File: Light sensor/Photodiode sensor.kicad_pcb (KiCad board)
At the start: 2 copper layers, 29.2 x 22.6 mm, 23 parts, among them IC1 MCP6002-E_MS, IC2 MCP6002-E_MS, J1 Conn_01x02, J2 Conn_01x05, J3 Conn_01x04

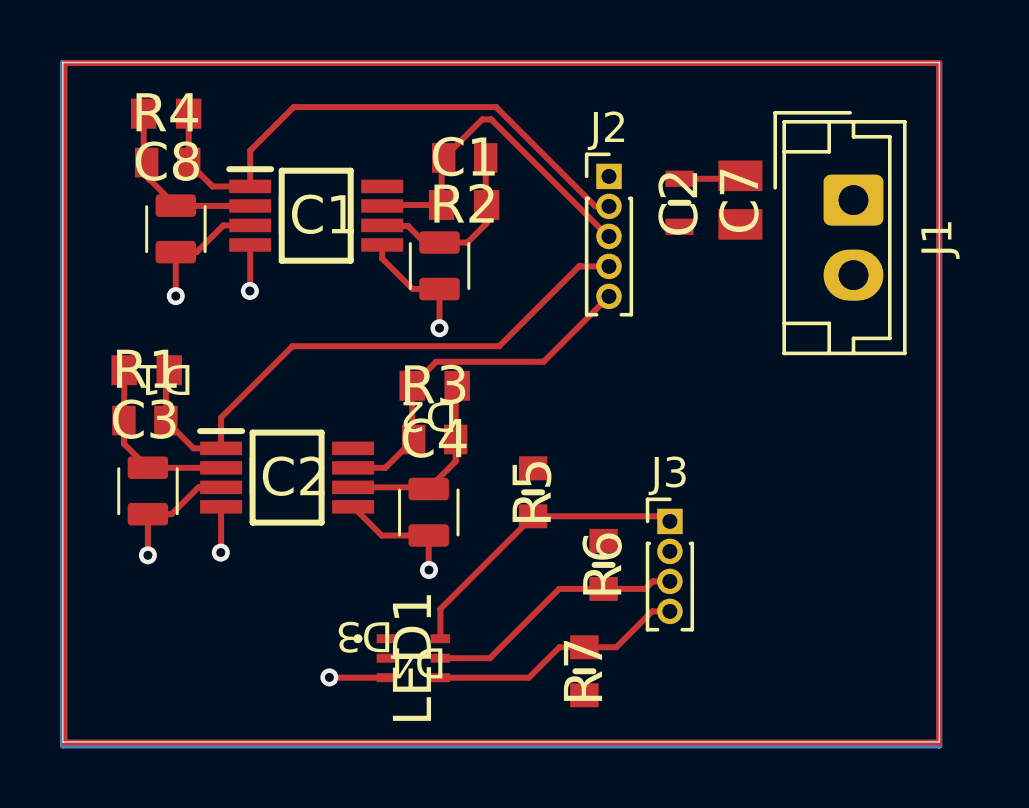
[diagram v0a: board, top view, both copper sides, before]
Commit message: V3 light sensor
It is the neatest one so far. It had a lot better EMC than originally thought for the 4 channel op amp
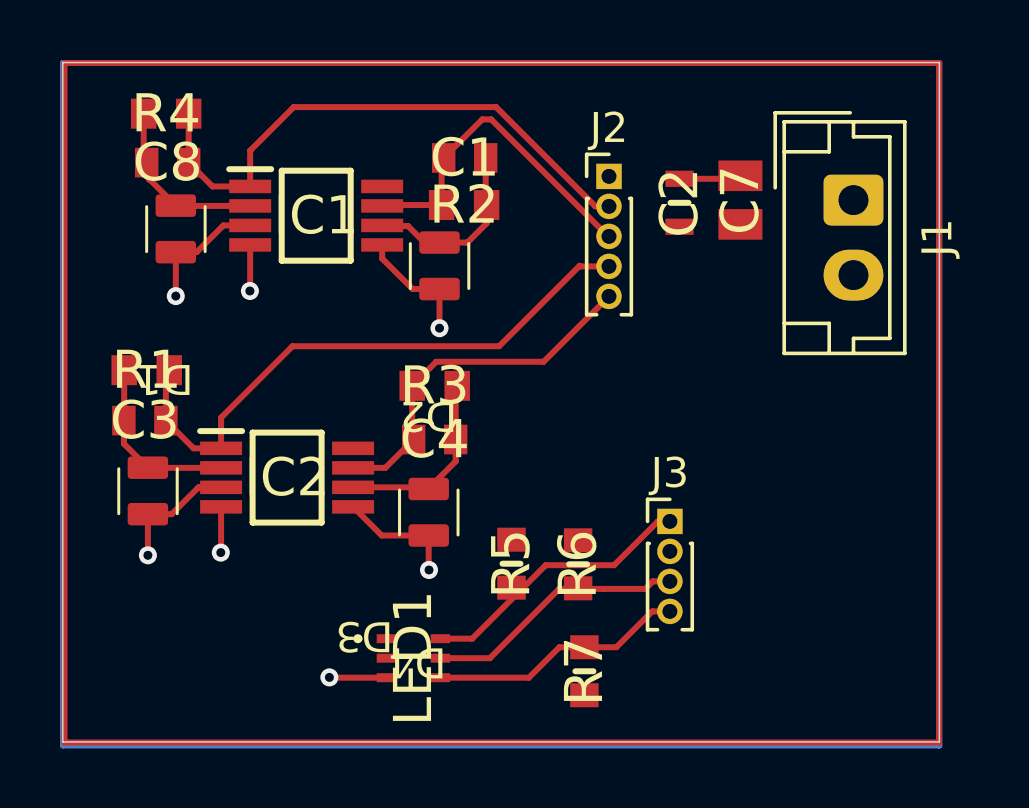
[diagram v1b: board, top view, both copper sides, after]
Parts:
- moved R5 2.49 mm to (127.0, 83.8)
- moved R6 0.85 mm to (129.3, 83.8)
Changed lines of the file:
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@@
 	(footprint "CUSTOM_LIBRARY:RESC1608X55N"
 		(layer "F.Cu")
-		(at 127.77 81.42 90)
+		(at 127.05 83.8 90)
 		(descr "RC0603")
 		(tags "Resistor")
@@
 	(footprint "CUSTOM_LIBRARY:RESC1608X55N"
 		(layer "F.Cu")
-		(at 130.12 83.84 90)
+		(at 129.27 83.82 90)
 		(descr "RC0603")
 		(tags "Resistor")
@@
 	)
 	(segment
-		(start 124.68 85.31)
-		(end 127.77 82.22)
+		(start 130.47 83.85)
+		(end 131.93 82.39)
 		(width 0.2)
 		(layer "F.Cu")
@@
 	(segment
 		(start 124.68 86.3)
-		(end 124.68 85.31)
+		(end 125.74 86.3)
 		(width 0.2)
 		(layer "F.Cu")
@@
 	)
 	(segment
-		(start 127.77 82.22)
-		(end 132.16 82.22)
+		(start 128.19 83.85)
+		(end 130.47 83.85)
+		(width 0.2)
+		(layer "F.Cu")
+		(net 12)
+	)
+	(segment
+		(start 125.74 86.3)
+		(end 128.19 83.85)
+		(width 0.2)
+		(layer "F.Cu")
+		(net 12)
+	)
+	(segment
+		(start 131.93 82.39)
+		(end 132.33 82.39)
 		(width 0.2)
 		(layer "F.Cu")
